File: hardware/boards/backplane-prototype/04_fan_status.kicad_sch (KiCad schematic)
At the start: 14 parts, among them J11 12V 3-WIRE FAN, J12 DS18B20 EXT SUPPLY, J9 12V 3-WIRE FAN, Q1 AO3407A, Q2 2N7002, Q3 AO3407A, Q4 2N7002

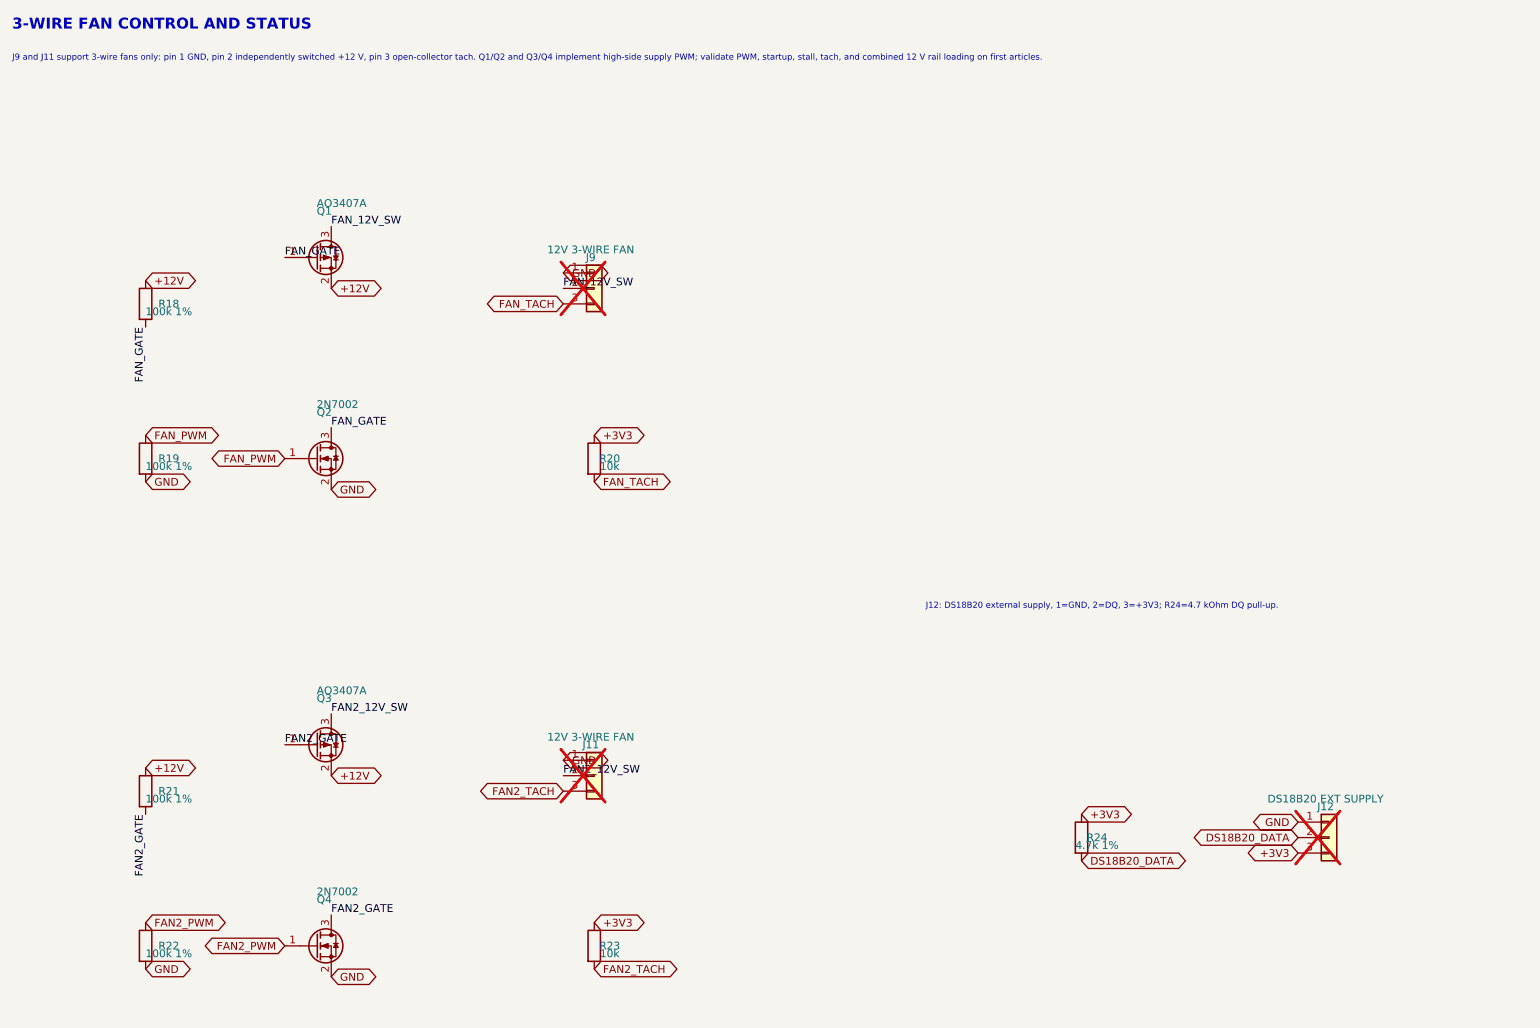
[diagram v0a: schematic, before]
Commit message: use official KiCad power symbols throughout backplane
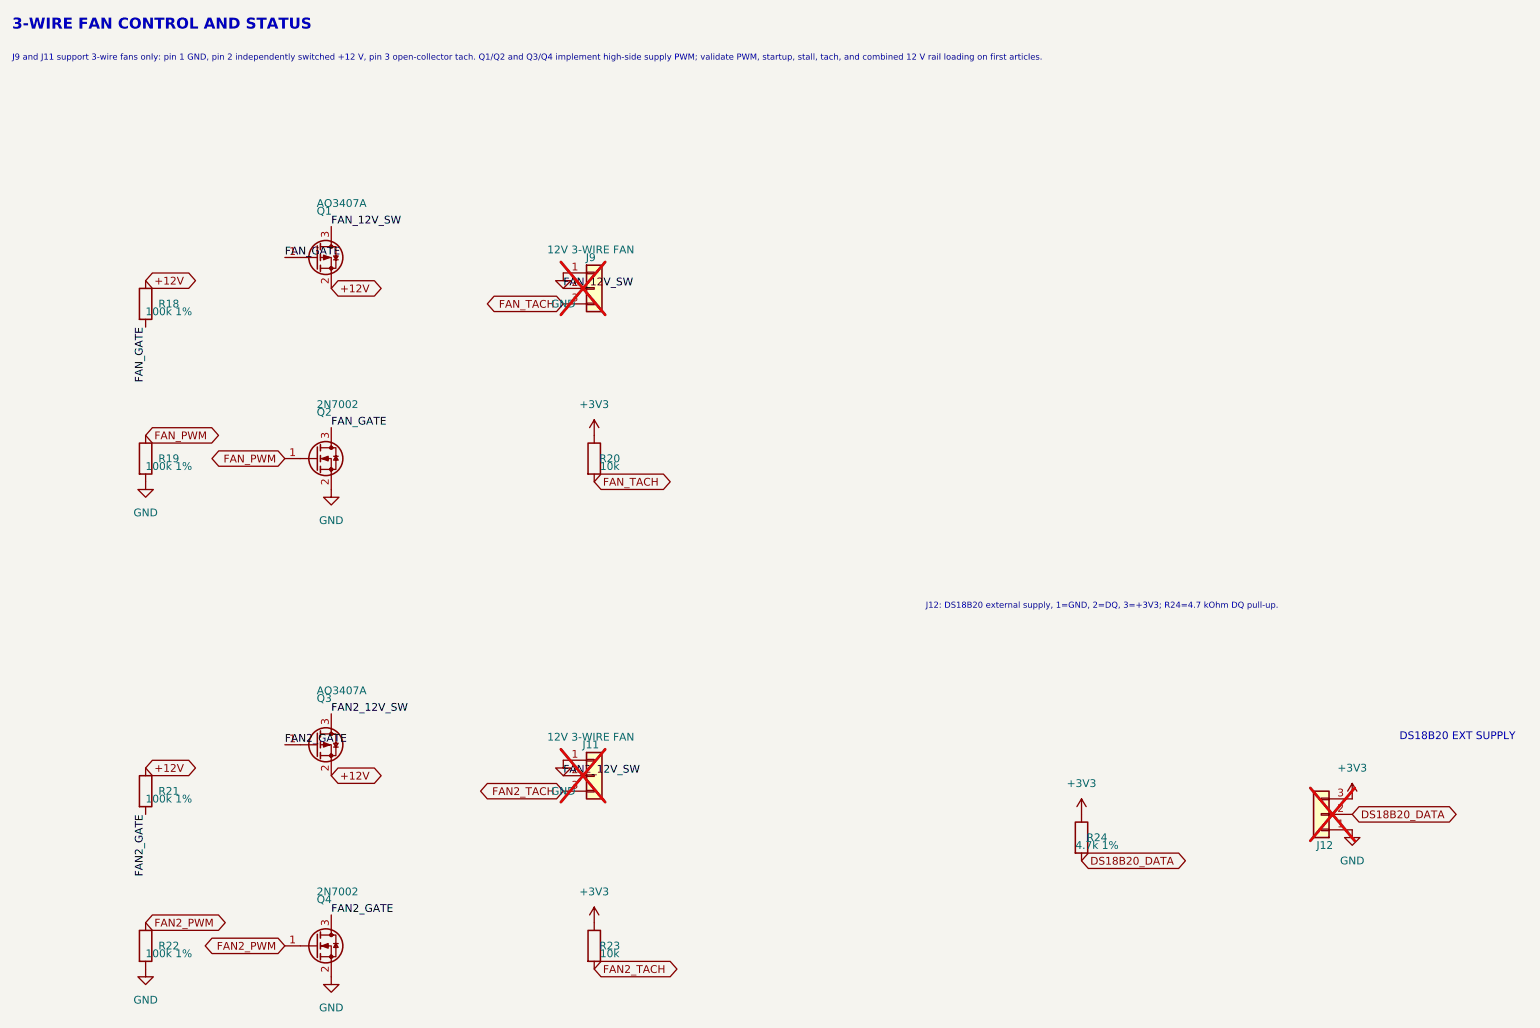
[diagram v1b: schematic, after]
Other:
- note added: "DS18B20 EXT SUPPLY"
- moved on the sheet: J12

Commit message: checkpoint before 12V and VCC power symbol conversion
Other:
- moved on the sheet: J11

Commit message: use official 12V and VCC power symbols
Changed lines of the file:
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@@
 		)
 	)
-	(global_label "+12V"
-		(shape bidirectional)
+	(symbol
+		(lib_id "power:+12V")
 		(at 41.91 58.42 0)
-		(effects
-			(font
-				(size 1.27 1.27)
-			)
-			(justify left)
-		)
-		(property "Intersheetrefs" "${INTERSHEET_REFS}"
+		(unit 1)
+		(body_style 1)
+		(exclude_from_sim no)
+		(in_bom yes)
+		(on_board yes)
+		(in_pos_files yes)
+		(dnp no)
+		(fields_autoplaced yes)
+		(property "Reference" "#PWR102"
+			(at 41.91 62.23 0)
+			(hide yes)
+			(show_name no)
+			(do_not_autoplace no)
+			(effects
+				(font
+					(size 1.27 1.27)
+				)
+			)
+		)
+		(property "Value" "+12V"
+			(at 41.91 53.34 0)
+			(show_name no)
+			(do_not_autoplace no)
+			(effects
+				(font
+					(size 1.27 1.27)
+				)
+			)
+		)
+		(property "Footprint" ""
 			(at 41.91 58.42 0)
 			(hide yes)
@@
 			)
 		)
+		(property "Datasheet" ""
+			(at 41.91 58.42 0)
+			(hide yes)
+			(show_name no)
+			(do_not_autoplace no)
+			(effects
+				(font
+					(size 1.27 1.27)
+				)
+			)
+		)
+		(property "Description" "Power symbol creates a global label with name \"+12V\""
+			(at 41.91 58.42 0)
+			(hide yes)
+			(show_name no)
+			(do_not_autoplace no)
+			(effects
+				(font
+					(size 1.27 1.27)
+				)
+			)
+		)
+		(pin "1"
+		)
+		(instances
+			(project "backplane-prototype"
+				(path "/348cc909-6345-4013-9bef-98714057a65b/5d5cc60b-4c39-4882-898d-1aa7068798ee"
+					(reference "#PWR102")
+					(unit 1)
+				)
+			)
+		)
 	)
 	(global_label "FAN2_PWM"
@@
 		)
 	)
-	(global_label "+12V"
-		(shape bidirectional)
+	(symbol
+		(lib_id "power:+12V")
 		(at 72.39 139.7 0)
-		(effects
-			(font
-				(size 1.27 1.27)
-			)
-			(justify left)
-		)
-		(property "Intersheetrefs" "${INTERSHEET_REFS}"
+		(unit 1)
+		(body_style 1)
+		(exclude_from_sim no)
+		(in_bom yes)
+		(on_board yes)
+		(in_pos_files yes)
+		(dnp no)
+		(fields_autoplaced yes)
+		(property "Reference" "#PWR103"
+			(at 72.39 143.51 0)
+			(hide yes)
+			(show_name no)
+			(do_not_autoplace no)
+			(effects
+				(font
+					(size 1.27 1.27)
+				)
+			)
+		)
+		(property "Value" "+12V"
+			(at 72.39 134.62 0)
+			(show_name no)
+			(do_not_autoplace no)
+			(effects
+				(font
+					(size 1.27 1.27)
+				)
+			)
+		)
+		(property "Footprint" ""
 			(at 72.39 139.7 0)
 			(hide yes)
@@
 			)
 		)
+		(property "Datasheet" ""
+			(at 72.39 139.7 0)
+			(hide yes)
+			(show_name no)
+			(do_not_autoplace no)
+			(effects
+				(font
+					(size 1.27 1.27)
+				)
+			)
+		)
+		(property "Description" "Power symbol creates a global label with name \"+12V\""
+			(at 72.39 139.7 0)
+			(hide yes)
+			(show_name no)
+			(do_not_autoplace no)
+			(effects
+				(font
+					(size 1.27 1.27)
+				)
+			)
+		)
+		(pin "1"
+		)
+		(instances
+			(project "backplane-prototype"
+				(path "/348cc909-6345-4013-9bef-98714057a65b/5d5cc60b-4c39-4882-898d-1aa7068798ee"
+					(reference "#PWR103")
+					(unit 1)
+				)
+			)
+		)
 	)
 	(global_label "DS18B20_DATA"
@@
 		)
 	)
-	(global_label "+12V"
-		(shape bidirectional)
+	(symbol
+		(lib_id "power:+12V")
 		(at 72.39 59.69 0)
-		(effects
-			(font
-				(size 1.27 1.27)
-			)
-			(justify left)
-		)
-		(property "Intersheetrefs" "${INTERSHEET_REFS}"
+		(unit 1)
+		(body_style 1)
+		(exclude_from_sim no)
+		(in_bom yes)
+		(on_board yes)
+		(in_pos_files yes)
+		(dnp no)
+		(fields_autoplaced yes)
+		(property "Reference" "#PWR104"
+			(at 72.39 63.5 0)
+			(hide yes)
+			(show_name no)
+			(do_not_autoplace no)
+			(effects
+				(font
+					(size 1.27 1.27)
+				)
+			)
+		)
+		(property "Value" "+12V"
+			(at 72.39 54.61 0)
+			(show_name no)
+			(do_not_autoplace no)
+			(effects
+				(font
+					(size 1.27 1.27)
+				)
+			)
+		)
+		(property "Footprint" ""
 			(at 72.39 59.69 0)
 			(hide yes)
@@
 				)
 			)
+		)
+		(property "Datasheet" ""
+			(at 72.39 59.69 0)
+			(hide yes)
+			(show_name no)
+			(do_not_autoplace no)
+			(effects
+				(font
+					(size 1.27 1.27)
+				)
+			)
+		)
+		(property "Description" "Power symbol creates a global label with name \"+12V\""
+			(at 72.39 59.69 0)
+			(hide yes)
+			(show_name no)
+			(do_not_autoplace no)
+			(effects
+				(font
+					(size 1.27 1.27)
+				)
+			)
+		)
+		(pin "1"
+		)
+		(instances
+			(project "backplane-prototype"
+				(path "/348cc909-6345-4013-9bef-98714057a65b/5d5cc60b-4c39-4882-898d-1aa7068798ee"
+					(reference "#PWR104")
+					(unit 1)
+				)
+			)
